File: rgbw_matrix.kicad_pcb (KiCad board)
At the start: 2 copper layers, 48 x 72 mm, 34 parts, among them IC1 TLC59283DBQR, IC2 TLC59283DBQR, IC3 TLC59283DBQR, IC4 TLC59283DBQR, IC5 TLC59283DBQR, IC6 TLC59283DBQR

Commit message: Did a little more schematic routing
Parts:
- turned IC1 to 0 degrees
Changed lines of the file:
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@@
   )
   (footprint "local:SOP64P600X175-24N" (layer "B.Cu")
-    (at 36.75 47 180)
+    (at 36.75 47)
     (descr "DBQ (R-PDSO-G24)")
     (tags "Integrated Circuit")
@@
     (fp_line (start -1.95 4.325) (end 1.95 4.325) (layer "B.Fab") (width 0.1))
     (fp_line (start -1.95 3.69) (end -1.315 4.325) (layer "B.Fab") (width 0.1))
-    (pad "1" smd rect (at -2.712 3.492 90) (size 0.435 1.525) (layers "B.Cu" "B.Paste" "B.Mask")
+    (pad "1" smd rect (at -2.712 3.492 270) (size 0.435 1.525) (layers "B.Cu" "B.Paste" "B.Mask")
       (net 6 "unconnected-(IC1-Pad1)") (pinfunction "GND") (pintype "power_in"))
-    (pad "2" smd rect (at -2.712 2.858 90) (size 0.435 1.525) (layers "B.Cu" "B.Paste" "B.Mask")
+    (pad "2" smd rect (at -2.712 2.858 270) (size 0.435 1.525) (layers "B.Cu" "B.Paste" "B.Mask")
       (net 7 "unconnected-(IC1-Pad2)") (pinfunction "SIN") (pintype "input"))
-    (pad "3" smd rect (at -2.712 2.222 90) (size 0.435 1.525) (layers "B.Cu" "B.Paste" "B.Mask")
+    (pad "3" smd rect (at -2.712 2.222 270) (size 0.435 1.525) (layers "B.Cu" "B.Paste" "B.Mask")
       (net 8 "unconnected-(IC1-Pad3)") (pinfunction "SCLK") (pintype "input"))
-    (pad "4" smd rect (at -2.712 1.588 90) (size 0.435 1.525) (layers "B.Cu" "B.Paste" "B.Mask")
+    (pad "4" smd rect (at -2.712 1.588 270) (size 0.435 1.525) (layers "B.Cu" "B.Paste" "B.Mask")
       (net 9 "unconnected-(IC1-Pad4)") (pinfunction "LAT") (pintype "input"))
-    (pad "5" smd rect (at -2.712 0.952 90) (size 0.435 1.525) (layers "B.Cu" "B.Paste" "B.Mask")
+    (pad "5" smd rect (at -2.712 0.952 270) (size 0.435 1.525) (layers "B.Cu" "B.Paste" "B.Mask")
       (net 98 "unconnected-(IC1-Pad5)") (pinfunction "OUT0") (pintype "output"))
-    (pad "6" smd rect (at -2.712 0.318 90) (size 0.435 1.525) (layers "B.Cu" "B.Paste" "B.Mask")
+    (pad "6" smd rect (at -2.712 0.318 270) (size 0.435 1.525) (layers "B.Cu" "B.Paste" "B.Mask")
       (net 10 "unconnected-(IC1-Pad6)") (pinfunction "OUT1") (pintype "output"))
-    (pad "7" smd rect (at -2.712 -0.318 90) (size 0.435 1.525) (layers "B.Cu" "B.Paste" "B.Mask")
+    (pad "7" smd rect (at -2.712 -0.318 270) (size 0.435 1.525) (layers "B.Cu" "B.Paste" "B.Mask")
       (net 11 "unconnected-(IC1-Pad7)") (pinfunction "OUT2") (pintype "output"))
-    (pad "8" smd rect (at -2.712 -0.952 90) (size 0.435 1.525) (layers "B.Cu" "B.Paste" "B.Mask")
+    (pad "8" smd rect (at -2.712 -0.952 270) (size 0.435 1.525) (layers "B.Cu" "B.Paste" "B.Mask")
       (net 12 "unconnected-(IC1-Pad8)") (pinfunction "OUT3") (pintype "output"))
-    (pad "9" smd rect (at -2.712 -1.588 90) (size 0.435 1.525) (layers "B.Cu" "B.Paste" "B.Mask")
+    (pad "9" smd rect (at -2.712 -1.588 270) (size 0.435 1.525) (layers "B.Cu" "B.Paste" "B.Mask")
       (net 13 "unconnected-(IC1-Pad9)") (pinfunction "OUT4") (pintype "output"))
-    (pad "10" smd rect (at -2.712 -2.222 90) (size 0.435 1.525) (layers "B.Cu" "B.Paste" "B.Mask")
+    (pad "10" smd rect (at -2.712 -2.222 270) (size 0.435 1.525) (layers "B.Cu" "B.Paste" "B.Mask")
       (net 14 "unconnected-(IC1-Pad10)") (pinfunction "OUT5") (pintype "output"))
-    (pad "11" smd rect (at -2.712 -2.858 90) (size 0.435 1.525) (layers "B.Cu" "B.Paste" "B.Mask")
+    (pad "11" smd rect (at -2.712 -2.858 270) (size 0.435 1.525) (layers "B.Cu" "B.Paste" "B.Mask")
       (net 15 "unconnected-(IC1-Pad11)") (pinfunction "OUT6") (pintype "output"))
-    (pad "12" smd rect (at -2.712 -3.492 90) (size 0.435 1.525) (layers "B.Cu" "B.Paste" "B.Mask")
+    (pad "12" smd rect (at -2.712 -3.492 270) (size 0.435 1.525) (layers "B.Cu" "B.Paste" "B.Mask")
       (net 16 "unconnected-(IC1-Pad12)") (pinfunction "OUT7") (pintype "output"))
-    (pad "13" smd rect (at 2.712 -3.492 90) (size 0.435 1.525) (layers "B.Cu" "B.Paste" "B.Mask")
+    (pad "13" smd rect (at 2.712 -3.492 270) (size 0.435 1.525) (layers "B.Cu" "B.Paste" "B.Mask")
       (net 17 "unconnected-(IC1-Pad13)") (pinfunction "OUT8") (pintype "output"))
-    (pad "14" smd rect (at 2.712 -2.858 90) (size 0.435 1.525) (layers "B.Cu" "B.Paste" "B.Mask")
+    (pad "14" smd rect (at 2.712 -2.858 270) (size 0.435 1.525) (layers "B.Cu" "B.Paste" "B.Mask")
       (net 18 "unconnected-(IC1-Pad14)") (pinfunction "OUT9") (pintype "output"))
-    (pad "15" smd rect (at 2.712 -2.222 90) (size 0.435 1.525) (layers "B.Cu" "B.Paste" "B.Mask")
+    (pad "15" smd rect (at 2.712 -2.222 270) (size 0.435 1.525) (layers "B.Cu" "B.Paste" "B.Mask")
       (net 19 "unconnected-(IC1-Pad15)") (pinfunction "OUT10") (pintype "output"))
-    (pad "16" smd rect (at 2.712 -1.588 90) (size 0.435 1.525) (layers "B.Cu" "B.Paste" "B.Mask")
+    (pad "16" smd rect (at 2.712 -1.588 270) (size 0.435 1.525) (layers "B.Cu" "B.Paste" "B.Mask")
       (net 20 "unconnected-(IC1-Pad16)") (pinfunction "OUT11") (pintype "output"))
-    (pad "17" smd rect (at 2.712 -0.952 90) (size 0.435 1.525) (layers "B.Cu" "B.Paste" "B.Mask")
+    (pad "17" smd rect (at 2.712 -0.952 270) (size 0.435 1.525) (layers "B.Cu" "B.Paste" "B.Mask")
       (net 21 "unconnected-(IC1-Pad17)") (pinfunction "OUT12") (pintype "output"))
-    (pad "18" smd rect (at 2.712 -0.318 90) (size 0.435 1.525) (layers "B.Cu" "B.Paste" "B.Mask")
+    (pad "18" smd rect (at 2.712 -0.318 270) (size 0.435 1.525) (layers "B.Cu" "B.Paste" "B.Mask")
       (net 22 "unconnected-(IC1-Pad18)") (pinfunction "OUT13") (pintype "output"))
-    (pad "19" smd rect (at 2.712 0.318 90) (size 0.435 1.525) (layers "B.Cu" "B.Paste" "B.Mask")
+    (pad "19" smd rect (at 2.712 0.318 270) (size 0.435 1.525) (layers "B.Cu" "B.Paste" "B.Mask")
       (net 23 "unconnected-(IC1-Pad19)") (pinfunction "OUT14") (pintype "output"))
-    (pad "20" smd rect (at 2.712 0.952 90) (size 0.435 1.525) (layers "B.Cu" "B.Paste" "B.Mask")
+    (pad "20" smd rect (at 2.712 0.952 270) (size 0.435 1.525) (layers "B.Cu" "B.Paste" "B.Mask")
       (net 24 "unconnected-(IC1-Pad20)") (pinfunction "OUT15") (pintype "output"))
-    (pad "21" smd rect (at 2.712 1.588 90) (size 0.435 1.525) (layers "B.Cu" "B.Paste" "B.Mask")
+    (pad "21" smd rect (at 2.712 1.588 270) (size 0.435 1.525) (layers "B.Cu" "B.Paste" "B.Mask")
       (net 25 "unconnected-(IC1-Pad21)") (pinfunction "BLANK") (pintype "input"))
-    (pad "22" smd rect (at 2.712 2.222 90) (size 0.435 1.525) (layers "B.Cu" "B.Paste" "B.Mask")
+    (pad "22" smd rect (at 2.712 2.222 270) (size 0.435 1.525) (layers "B.Cu" "B.Paste" "B.Mask")
       (net 26 "unconnected-(IC1-Pad22)") (pinfunction "SOUT") (pintype "output"))
-    (pad "23" smd rect (at 2.712 2.858 90) (size 0.435 1.525) (layers "B.Cu" "B.Paste" "B.Mask")
+    (pad "23" smd rect (at 2.712 2.858 270) (size 0.435 1.525) (layers "B.Cu" "B.Paste" "B.Mask")
       (net 27 "unconnected-(IC1-Pad23)") (pinfunction "IREF") (pintype "input"))
-    (pad "24" smd rect (at 2.712 3.492 90) (size 0.435 1.525) (layers "B.Cu" "B.Paste" "B.Mask")
+    (pad "24" smd rect (at 2.712 3.492 270) (size 0.435 1.525) (layers "B.Cu" "B.Paste" "B.Mask")
       (net 28 "unconnected-(IC1-Pad24)") (pinfunction "VCC") (pintype "power_in"))
     (model "${KIPRJMOD}/3d/TLC59283DBQR.stp"
@@
     (pts (xy 25 25) (xy 73 25))
     (height -6.5)
-    (gr_text "48.0000 mm" (at 49 17.35) (layer "User.1")
+    (gr_text "1.8898 in" (at 49 17.35) (layer "User.1")
       (effects (font (size 1 1) (thickness 0.15)))
     )
@@
     (pts (xy 25 25) (xy 25 97))
     (height 6.5)
-    (gr_text "72.0000 mm" (at 17.35 61 90) (layer "User.1")
+    (gr_text "2.8346 in" (at 17.35 61 90) (layer "User.1")
       (effects (font (size 1 1) (thickness 0.15)))
     )

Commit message: components connected v1
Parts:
- added C1: 1u, Capacitor_SMD:C_0201_0603Metric, B.Cu at (53.8, 35.4)
- added C2: 1u, Capacitor_SMD:C_0201_0603Metric, B.Cu at (53.8, 46.3)
- added C3: 1u, Capacitor_SMD:C_0201_0603Metric, B.Cu at (53.8, 57.1)
- added C4: 1u, Capacitor_SMD:C_0201_0603Metric, B.Cu at (53.8, 72.7)
- added C5: 1u, Capacitor_SMD:C_0201_0603Metric, B.Cu at (53.8, 83.6)
- added C6: 1u, Capacitor_SMD:C_0201_0603Metric, B.Cu at (53.8, 94.4)
- added J1: Conn_01x07_Female, Connector_PinHeader_2.54mm:PinHeader_1x07_P2.54mm_Vertical, F.Cu at (56.6, 61.0)
- added R1: 1.8k, Resistor_SMD:R_0201_0603Metric, B.Cu at (53.8, 34.1)
- added R2: 1.8k, Resistor_SMD:R_0201_0603Metric, B.Cu at (53.8, 44.9)
- added R3: 1.8k, Resistor_SMD:R_0201_0603Metric, B.Cu at (53.8, 55.8)
- added R4: 1.8k, Resistor_SMD:R_0201_0603Metric, B.Cu at (53.8, 71.4)
- added R5: 1.8k, Resistor_SMD:R_0201_0603Metric, B.Cu at (53.8, 82.3)
- added R6: 1.8k, Resistor_SMD:R_0201_0603Metric, B.Cu at (53.8, 93.0)
- moved IC1 19.8 mm to (49.0, 31.5)
- moved IC6 19.4 mm to (49.0, 90.5), turned to 0 degrees
- moved IC3 14.5 mm to (49.0, 53.2), turned to 0 degrees
- moved IC4 14.4 mm to (49.0, 68.8), turned to 0 degrees
- moved IC2 13.0 mm to (49.0, 42.3), turned to 0 degrees
- moved IC5 13.0 mm to (49.0, 79.7), turned to 0 degrees
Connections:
- D1 pad 1: D1R -> D1W
- D1 pad 2: unconnected-(D1-Pad2) -> D1B
- D1 pad 3: unconnected-(D1-Pad3) -> D1G
- D1 pad 4: unconnected-(D1-Pad4) -> D1R
- D10 pad 1: D1R -> D10W
- D10 pad 2: unconnected-(D10-Pad2) -> D10B
- D10 pad 3: unconnected-(D10-Pad3) -> D10G
- D10 pad 4: unconnected-(D10-Pad4) -> D10R
- D11 pad 1: D1R -> D11W
- D11 pad 2: unconnected-(D11-Pad2) -> D11B
- D11 pad 3: unconnected-(D11-Pad3) -> D11G
- D11 pad 4: unconnected-(D11-Pad4) -> D11R
- D12 pad 1: D1R -> D12W
- D12 pad 2: unconnected-(D12-Pad2) -> D12B
- D12 pad 3: unconnected-(D12-Pad3) -> D12G
- D12 pad 4: unconnected-(D12-Pad4) -> D12R
- D13 pad 1: D1R -> D13W
- D13 pad 2: unconnected-(D13-Pad2) -> D13B
- D13 pad 3: unconnected-(D13-Pad3) -> D13G
- D13 pad 4: unconnected-(D13-Pad4) -> D13R
- D14 pad 1: D1R -> D14W
- D14 pad 2: unconnected-(D14-Pad2) -> D14B
- D14 pad 3: unconnected-(D14-Pad3) -> D14G
- D14 pad 4: unconnected-(D14-Pad4) -> D14R
- D15 pad 1: D1R -> D15W
- D15 pad 2: unconnected-(D15-Pad2) -> D15B
- D15 pad 3: unconnected-(D15-Pad3) -> D15G
- D15 pad 4: unconnected-(D15-Pad4) -> D15R
- D16 pad 1: D1R -> D16W
- D16 pad 2: unconnected-(D16-Pad2) -> D16B
- D16 pad 3: unconnected-(D16-Pad3) -> D16G
- D16 pad 4: unconnected-(D16-Pad4) -> D16R
- D17 pad 1: D1R -> D17W
- D17 pad 2: unconnected-(D17-Pad2) -> D17B
- D17 pad 3: unconnected-(D17-Pad3) -> D17G
- D17 pad 4: unconnected-(D17-Pad4) -> D17R
- D18 pad 1: D1R -> D18W
- D18 pad 2: unconnected-(D18-Pad2) -> D18B
- D18 pad 3: unconnected-(D18-Pad3) -> D18G
- D18 pad 4: unconnected-(D18-Pad4) -> D18R
- D19 pad 1: D1R -> D19W
- D19 pad 2: unconnected-(D19-Pad2) -> D19B
- D19 pad 3: unconnected-(D19-Pad3) -> D19G
- D19 pad 4: unconnected-(D19-Pad4) -> D19R
- D2 pad 1: D1R -> D2W
- D2 pad 2: unconnected-(D2-Pad2) -> D2B
- D2 pad 3: unconnected-(D2-Pad3) -> D2G
- D2 pad 4: unconnected-(D2-Pad4) -> D2R
- D20 pad 1: D1R -> D20W
- D20 pad 2: unconnected-(D20-Pad2) -> D20B
- D20 pad 3: unconnected-(D20-Pad3) -> D20G
- D20 pad 4: unconnected-(D20-Pad4) -> D20R
- D21 pad 1: D1R -> D21W
- D21 pad 2: unconnected-(D21-Pad2) -> D21B
- D21 pad 3: unconnected-(D21-Pad3) -> D21G
- D21 pad 4: unconnected-(D21-Pad4) -> D21R
- D22 pad 1: D1R -> D22W
- D22 pad 2: unconnected-(D22-Pad2) -> D22B
- D22 pad 3: unconnected-(D22-Pad3) -> D22G
- D22 pad 4: unconnected-(D22-Pad4) -> D22R
- D23 pad 1: D1R -> D23W
- D23 pad 2: unconnected-(D23-Pad2) -> D23B
- D23 pad 3: unconnected-(D23-Pad3) -> D23G
- D23 pad 4: unconnected-(D23-Pad4) -> D23R
- D24 pad 1: D1R -> D24W
- D24 pad 2: unconnected-(D24-Pad2) -> D24B
- D24 pad 3: unconnected-(D24-Pad3) -> D24G
- D24 pad 4: unconnected-(D24-Pad4) -> D24R
- D3 pad 1: D1R -> D3W
- D3 pad 2: unconnected-(D3-Pad2) -> D3B
- D3 pad 3: unconnected-(D3-Pad3) -> D3G
- D3 pad 4: unconnected-(D3-Pad4) -> D3R
- D4 pad 1: D1R -> D4W
- D4 pad 2: unconnected-(D4-Pad2) -> D4B
- D4 pad 3: unconnected-(D4-Pad3) -> D4G
- D4 pad 4: unconnected-(D4-Pad4) -> D4R
- D5 pad 1: D1R -> D5W
- D5 pad 2: unconnected-(D5-Pad2) -> D5B
- D5 pad 3: unconnected-(D5-Pad3) -> D5G
- D5 pad 4: unconnected-(D5-Pad4) -> D5R
- D6 pad 1: D1R -> D6W
- D6 pad 2: unconnected-(D6-Pad2) -> D6B
- D6 pad 3: unconnected-(D6-Pad3) -> D6G
- D6 pad 4: unconnected-(D6-Pad4) -> D6R
- D7 pad 1: D1R -> D7W
- D7 pad 2: unconnected-(D7-Pad2) -> D7B
- D7 pad 3: unconnected-(D7-Pad3) -> D7G
- D7 pad 4: unconnected-(D7-Pad4) -> D7R
- D8 pad 1: D1R -> D8W
- D8 pad 2: unconnected-(D8-Pad2) -> D8B
- D8 pad 3: unconnected-(D8-Pad3) -> D8G
- D8 pad 4: unconnected-(D8-Pad4) -> D8R
- D9 pad 1: D1R -> D9W
- D9 pad 2: unconnected-(D9-Pad2) -> D9B
- D9 pad 3: unconnected-(D9-Pad3) -> D9G
- D9 pad 4: unconnected-(D9-Pad4) -> D9R
- IC1 pad 1: unconnected-(IC1-Pad1) -> GND
- IC1 pad 10: unconnected-(IC1-Pad10) -> D2B
- IC1 pad 11: unconnected-(IC1-Pad11) -> D2G
- IC1 pad 12: unconnected-(IC1-Pad12) -> D2R
- IC1 pad 13: unconnected-(IC1-Pad13) -> D3W
- IC1 pad 14: unconnected-(IC1-Pad14) -> D3B
- IC1 pad 15: unconnected-(IC1-Pad15) -> D3G
- IC1 pad 16: unconnected-(IC1-Pad16) -> D3R
- IC1 pad 17: unconnected-(IC1-Pad17) -> D4W
- IC1 pad 18: unconnected-(IC1-Pad18) -> D4B
- IC1 pad 19: unconnected-(IC1-Pad19) -> D4G
- IC1 pad 2: unconnected-(IC1-Pad2) -> SIN
- IC1 pad 20: unconnected-(IC1-Pad20) -> D4R
- IC1 pad 21: unconnected-(IC1-Pad21) -> BLANK
- IC1 pad 22: unconnected-(IC1-Pad22) -> Net-(IC1-Pad22)
- IC1 pad 23: unconnected-(IC1-Pad23) -> Net-(IC1-Pad23)
- IC1 pad 24: unconnected-(IC1-Pad24) -> Net-(C1-Pad1)
- IC1 pad 3: unconnected-(IC1-Pad3) -> SCLK
- IC1 pad 4: unconnected-(IC1-Pad4) -> LAT
- IC1 pad 5: unconnected-(IC1-Pad5) -> D1W
- IC1 pad 6: unconnected-(IC1-Pad6) -> D1B
- IC1 pad 7: unconnected-(IC1-Pad7) -> D1G
- IC1 pad 8: unconnected-(IC1-Pad8) -> D1R
- IC1 pad 9: unconnected-(IC1-Pad9) -> D2W
- IC2 pad 1: unconnected-(IC2-Pad1) -> GND
- IC2 pad 10: unconnected-(IC2-Pad10) -> D6B
- IC2 pad 11: unconnected-(IC2-Pad11) -> D6G
- IC2 pad 12: unconnected-(IC2-Pad12) -> D6R
- IC2 pad 13: unconnected-(IC2-Pad13) -> D7W
- IC2 pad 14: unconnected-(IC2-Pad14) -> D7B
- IC2 pad 15: unconnected-(IC2-Pad15) -> D7G
- IC2 pad 16: unconnected-(IC2-Pad16) -> D7R
- IC2 pad 17: unconnected-(IC2-Pad17) -> D8W
- IC2 pad 18: unconnected-(IC2-Pad18) -> D8B
- IC2 pad 19: unconnected-(IC2-Pad19) -> D8G
- IC2 pad 2: unconnected-(IC2-Pad2) -> Net-(IC1-Pad22)
- IC2 pad 20: unconnected-(IC2-Pad20) -> D8R
- IC2 pad 21: unconnected-(IC2-Pad21) -> BLANK
- IC2 pad 22: unconnected-(IC2-Pad22) -> Net-(IC3-Pad2)
- IC2 pad 23: unconnected-(IC2-Pad23) -> Net-(IC2-Pad23)
- IC2 pad 24: unconnected-(IC2-Pad24) -> Net-(IC2-Pad24)
- IC2 pad 3: unconnected-(IC2-Pad3) -> SCLK
- IC2 pad 4: unconnected-(IC2-Pad4) -> LAT
- IC2 pad 5: unconnected-(IC2-Pad5) -> D5W
- IC2 pad 6: unconnected-(IC2-Pad6) -> D5B
- IC2 pad 7: unconnected-(IC2-Pad7) -> D5G
- IC2 pad 8: unconnected-(IC2-Pad8) -> D5R
- IC2 pad 9: unconnected-(IC2-Pad9) -> D6W
- IC3 pad 1: unconnected-(IC3-Pad1) -> GND
- IC3 pad 10: unconnected-(IC3-Pad10) -> D10B
- IC3 pad 11: unconnected-(IC3-Pad11) -> D10G
- IC3 pad 12: unconnected-(IC3-Pad12) -> D10R
- IC3 pad 13: unconnected-(IC3-Pad13) -> D11W
- IC3 pad 14: unconnected-(IC3-Pad14) -> D11B
- IC3 pad 15: unconnected-(IC3-Pad15) -> D11G
- IC3 pad 16: unconnected-(IC3-Pad16) -> D11R
- IC3 pad 17: unconnected-(IC3-Pad17) -> D12W
- IC3 pad 18: unconnected-(IC3-Pad18) -> D12B
- IC3 pad 19: unconnected-(IC3-Pad19) -> D12G
- IC3 pad 2: unconnected-(IC3-Pad2) -> Net-(IC3-Pad2)
- IC3 pad 20: unconnected-(IC3-Pad20) -> D12R
- IC3 pad 21: unconnected-(IC3-Pad21) -> BLANK
- IC3 pad 22: unconnected-(IC3-Pad22) -> Net-(IC3-Pad22)
- IC3 pad 23: unconnected-(IC3-Pad23) -> Net-(IC3-Pad23)
- IC3 pad 24: unconnected-(IC3-Pad24) -> Net-(IC3-Pad24)
- IC3 pad 3: unconnected-(IC3-Pad3) -> SCLK
- IC3 pad 4: unconnected-(IC3-Pad4) -> LAT
- IC3 pad 5: unconnected-(IC3-Pad5) -> D9W
- IC3 pad 6: unconnected-(IC3-Pad6) -> D9B
- IC3 pad 7: unconnected-(IC3-Pad7) -> D9G
- IC3 pad 8: unconnected-(IC3-Pad8) -> D9R
- IC3 pad 9: unconnected-(IC3-Pad9) -> D10W
- IC4 pad 1: unconnected-(IC4-Pad1) -> GND
- IC4 pad 10: unconnected-(IC4-Pad10) -> D14B
- IC4 pad 11: unconnected-(IC4-Pad11) -> D14G
- IC4 pad 12: unconnected-(IC4-Pad12) -> D14R
- IC4 pad 13: unconnected-(IC4-Pad13) -> D15W
- IC4 pad 14: unconnected-(IC4-Pad14) -> D15B
- IC4 pad 15: unconnected-(IC4-Pad15) -> D15G
- IC4 pad 16: unconnected-(IC4-Pad16) -> D15R
- IC4 pad 17: unconnected-(IC4-Pad17) -> D16W
- IC4 pad 18: unconnected-(IC4-Pad18) -> D16B
- IC4 pad 19: unconnected-(IC4-Pad19) -> D16G
- IC4 pad 2: unconnected-(IC4-Pad2) -> Net-(IC3-Pad22)
- IC4 pad 20: unconnected-(IC4-Pad20) -> D16R
- IC4 pad 21: unconnected-(IC4-Pad21) -> BLANK
- IC4 pad 22: unconnected-(IC4-Pad22) -> Net-(IC4-Pad22)
- IC4 pad 23: unconnected-(IC4-Pad23) -> Net-(IC4-Pad23)
- IC4 pad 24: unconnected-(IC4-Pad24) -> Net-(IC4-Pad24)
- IC4 pad 3: unconnected-(IC4-Pad3) -> SCLK
- IC4 pad 4: unconnected-(IC4-Pad4) -> LAT
- IC4 pad 5: unconnected-(IC4-Pad5) -> D13W
- IC4 pad 6: unconnected-(IC4-Pad6) -> D13B
- IC4 pad 7: unconnected-(IC4-Pad7) -> D13G
- IC4 pad 8: unconnected-(IC4-Pad8) -> D13R
- IC4 pad 9: unconnected-(IC4-Pad9) -> D14W
- IC5 pad 1: unconnected-(IC5-Pad1) -> GND
- IC5 pad 10: unconnected-(IC5-Pad10) -> D18B
- IC5 pad 11: unconnected-(IC5-Pad11) -> D18G
- IC5 pad 12: unconnected-(IC5-Pad12) -> D18R
- IC5 pad 13: unconnected-(IC5-Pad13) -> D19W
- IC5 pad 14: unconnected-(IC5-Pad14) -> D19B
- IC5 pad 15: unconnected-(IC5-Pad15) -> D19G
- IC5 pad 16: unconnected-(IC5-Pad16) -> D19R
- IC5 pad 17: unconnected-(IC5-Pad17) -> D20W
- IC5 pad 18: unconnected-(IC5-Pad18) -> D20B
- IC5 pad 19: unconnected-(IC5-Pad19) -> D20G
- IC5 pad 2: unconnected-(IC5-Pad2) -> Net-(IC4-Pad22)
- IC5 pad 20: unconnected-(IC5-Pad20) -> D20R
- IC5 pad 21: unconnected-(IC5-Pad21) -> BLANK
- IC5 pad 22: unconnected-(IC5-Pad22) -> Net-(IC6-Pad2)
- IC5 pad 23: unconnected-(IC5-Pad23) -> Net-(IC5-Pad23)
- IC5 pad 24: unconnected-(IC5-Pad24) -> Net-(IC5-Pad24)
- IC5 pad 3: unconnected-(IC5-Pad3) -> SCLK
- IC5 pad 4: unconnected-(IC5-Pad4) -> LAT
- IC5 pad 5: unconnected-(IC5-Pad5) -> D17W
- IC5 pad 6: unconnected-(IC5-Pad6) -> D17B
- IC5 pad 7: unconnected-(IC5-Pad7) -> D17G
- IC5 pad 8: unconnected-(IC5-Pad8) -> D17R
- IC5 pad 9: unconnected-(IC5-Pad9) -> D18W
- IC6 pad 1: unconnected-(IC6-Pad1) -> GND
- IC6 pad 10: unconnected-(IC6-Pad10) -> D22B
- IC6 pad 11: unconnected-(IC6-Pad11) -> D22G
- IC6 pad 12: unconnected-(IC6-Pad12) -> D22R
- IC6 pad 13: unconnected-(IC6-Pad13) -> D23W
- IC6 pad 14: unconnected-(IC6-Pad14) -> D23B
- IC6 pad 15: unconnected-(IC6-Pad15) -> D23G
- IC6 pad 16: unconnected-(IC6-Pad16) -> D23R
- IC6 pad 17: unconnected-(IC6-Pad17) -> D24W
- IC6 pad 18: unconnected-(IC6-Pad18) -> D24B
- IC6 pad 19: unconnected-(IC6-Pad19) -> D24G
- IC6 pad 2: unconnected-(IC6-Pad2) -> Net-(IC6-Pad2)
- IC6 pad 20: unconnected-(IC6-Pad20) -> D24R
- IC6 pad 21: unconnected-(IC6-Pad21) -> BLANK
- IC6 pad 22: unconnected-(IC6-Pad22) -> SOUT
- IC6 pad 23: unconnected-(IC6-Pad23) -> Net-(IC6-Pad23)
- IC6 pad 24: unconnected-(IC6-Pad24) -> Net-(IC6-Pad24)
- IC6 pad 3: unconnected-(IC6-Pad3) -> SCLK
- IC6 pad 4: unconnected-(IC6-Pad4) -> LAT
- IC6 pad 5: unconnected-(IC6-Pad5) -> D21W
- IC6 pad 6: unconnected-(IC6-Pad6) -> D21B
- IC6 pad 7: unconnected-(IC6-Pad7) -> D21G
- IC6 pad 8: unconnected-(IC6-Pad8) -> D21R
- IC6 pad 9: unconnected-(IC6-Pad9) -> D22W
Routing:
- net SCLK: track 0.00 -> 79.3 mm, vias 0 -> 6
- net BLANK: track 0.00 -> 74.5 mm, vias 0 -> 6
- net LAT: track 0.00 -> 71.5 mm, vias 0 -> 6
- net SOUT: track 0.00 -> 39.0 mm, vias 0 -> 1
- net Net-(IC3-Pad22): track 0.00 -> 35.2 mm
- net SIN: track 0.00 -> 28.5 mm, vias 0 -> 1
- net D12R: track 0.00 -> 22.2 mm, vias 0 -> 1
- net D9W: track 0.00 -> 22.0 mm, vias 0 -> 1
- net D24R: track 0.00 -> 21.7 mm, vias 0 -> 1
- net D8R: track 0.00 -> 21.6 mm, vias 0 -> 1
- net D5W: track 0.00 -> 21.4 mm, vias 0 -> 1
- net D17W: track 0.00 -> 21.2 mm, vias 0 -> 1
- net D20R: track 0.00 -> 21.1 mm, vias 0 -> 1
- net D4R: track 0.00 -> 21.0 mm, vias 0 -> 1
- net D7R: track 0.00 -> 21.0 mm, vias 0 -> 1
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- added copper zone on B.Cu, net GND
- added copper zone on F.Cu, net VCC

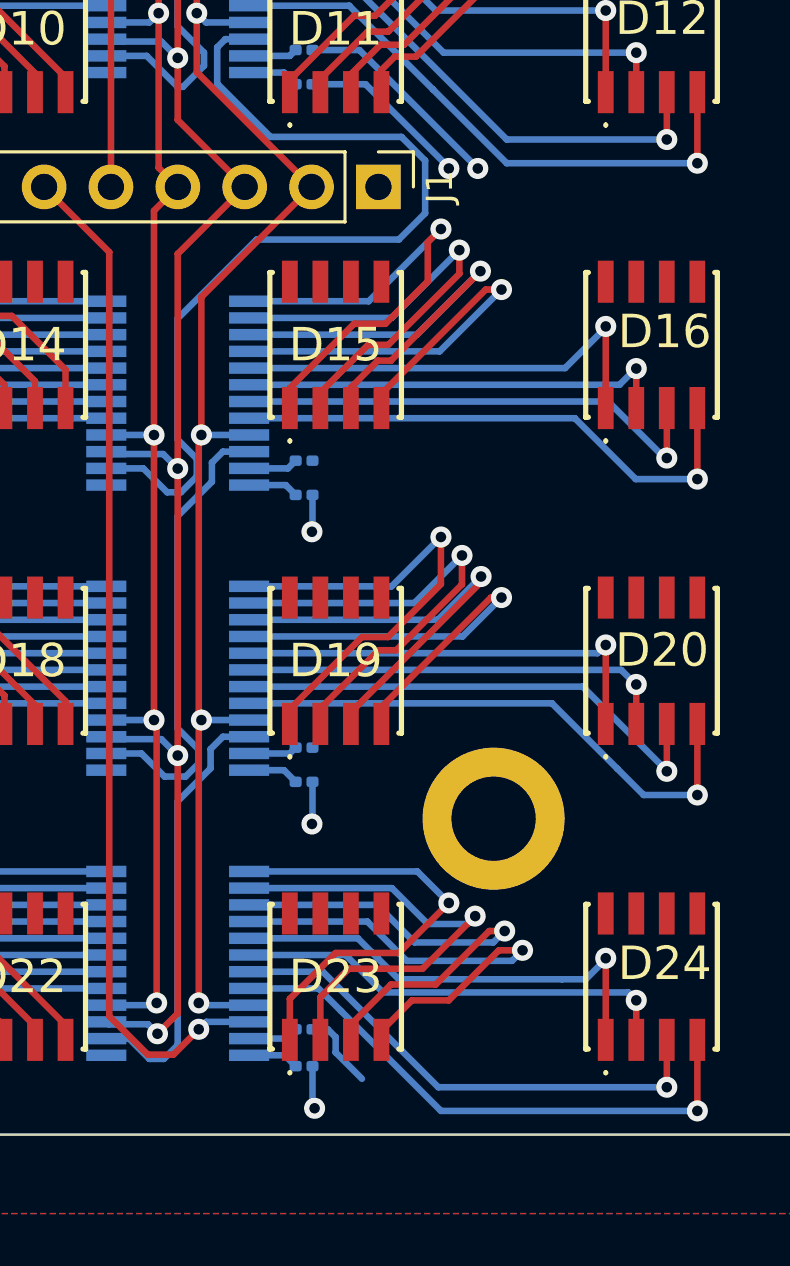
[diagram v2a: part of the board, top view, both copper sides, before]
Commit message: components connected v1.1
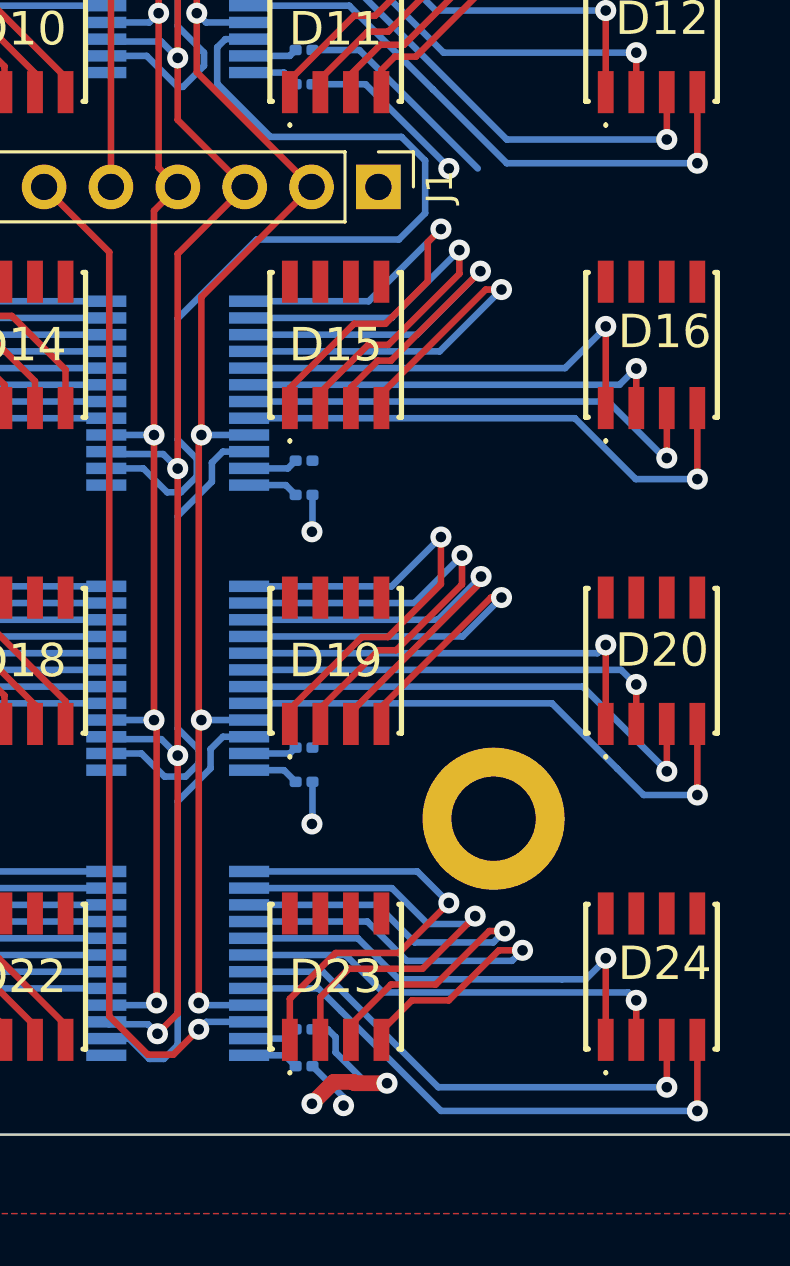
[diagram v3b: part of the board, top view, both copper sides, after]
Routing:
- net GND: track 15.0 -> 18.3 mm, vias 3 -> 4
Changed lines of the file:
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@@
   (via (at 56 48) (size 0.8) (drill 0.4) (layers "F.Cu" "B.Cu") (net 5))
   (via (at 54.1 74.1) (size 0.8) (drill 0.4) (layers "F.Cu" "B.Cu") (net 5))
-  (via (at 54.2 96) (size 0.8) (drill 0.4) (layers "F.Cu" "B.Cu") (net 5))
+  (via (at 55.3 95.8995) (size 0.8) (drill 0.4) (layers "F.Cu" "B.Cu") (net 5))
   (via (at 59.3 60.3) (size 0.8) (drill 0.4) (layers "F.Cu" "B.Cu") (net 5))
   (via (at 54.1 85.2) (size 0.8) (drill 0.4) (layers "F.Cu" "B.Cu") (net 5))
@@
   (segment (start 54.12 35.4) (end 54.12 37.12) (width 0.25) (layer "B.Cu") (net 5))
   (segment (start 54.12 74.08) (end 54.1 74.1) (width 0.25) (layer "B.Cu") (net 5))
-  (segment (start 54.12 95.92) (end 54.2 96) (width 0.25) (layer "B.Cu") (net 5))
+  (segment (start 55.3 95.58) (end 54.12 94.4) (width 0.25) (layer "B.Cu") (net 5))
   (segment (start 54.12 46.3) (end 54.3 46.3) (width 0.25) (layer "B.Cu") (net 5))
-  (segment (start 54.12 94.4) (end 54.12 95.92) (width 0.25) (layer "B.Cu") (net 5))
   (segment (start 54.12 37.12) (end 54.2 37.2) (width 0.25) (layer "B.Cu") (net 5))
+  (segment (start 55.3 95.8995) (end 55.3 95.58) (width 0.25) (layer "B.Cu") (net 5))
   (segment (start 59.3 60.263604) (end 56.136396 57.1) (width 0.25) (layer "B.Cu") (net 5))
   (segment (start 54.12 85.18) (end 54.1 85.2) (width 0.25) (layer "B.Cu") (net 5))
@@
   (segment (start 49 48.1) (end 50.4 46.7) (width 0.25) (layer "B.Cu") (net 119))
   (segment (start 49.2 57.2) (end 50 56.4) (width 0.25) (layer "B.Cu") (net 119))
+  (segment (start 55.672793 94.9995) (end 54.927207 94.9995) (width 0.6) (layer "F.Cu") (net 120))
+  (segment (start 56.951843 95.048157) (end 55.72145 95.048157) (width 0.6) (layer "F.Cu") (net 120))
+  (segment (start 54.927207 94.9995) (end 54.1 95.826707) (width 0.6) (layer "F.Cu") (net 120))
+  (segment (start 55.72145 95.048157) (end 55.672793 94.9995) (width 0.6) (layer "F.Cu") (net 120))
   (segment (start 39.7 95.9) (end 39.2 95.9) (width 1.2) (layer "F.Cu") (net 120))
   (segment (start 39.2 95.9) (end 36.8 93.5) (width 1.2) (layer "F.Cu") (net 120))
   (via (at 39.7 95.9) (size 0.8) (drill 0.4) (layers "F.Cu" "B.Cu") (free) (net 120))
-  (via (at 60.4 60.3) (size 0.8) (drill 0.4) (layers "F.Cu" "B.Cu") (net 120))
+  (via (at 56.951843 95.048157) (size 0.8) (drill 0.4) (layers "F.Cu" "B.Cu") (free) (net 120))
   (via (at 36.8 93.5) (size 0.8) (drill 0.4) (layers "F.Cu" "B.Cu") (free) (net 120))
+  (via (at 54.1 95.826707) (size 0.8) (drill 0.4) (layers "F.Cu" "B.Cu") (free) (net 120))
   (segment (start 55 93.3) (end 55 93.88) (width 0.25) (layer "B.Cu") (net 120))
   (segment (start 54.12 55.8) (end 55.9 55.8) (width 0.25) (layer "B.Cu") (net 120))
